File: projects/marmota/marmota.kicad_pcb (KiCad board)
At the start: 2 copper layers, 70 x 70 mm, 59 parts, among them J1 USB_C, J2 Conn_01x20_Pin, J3 Conn_01x20_Pin, SW1 Button top, SW2 Button side, U1 RP2040, U2 FLASH, U3 MCP73871, U4 RT6160, U5 ESP32, Y1 12MHz

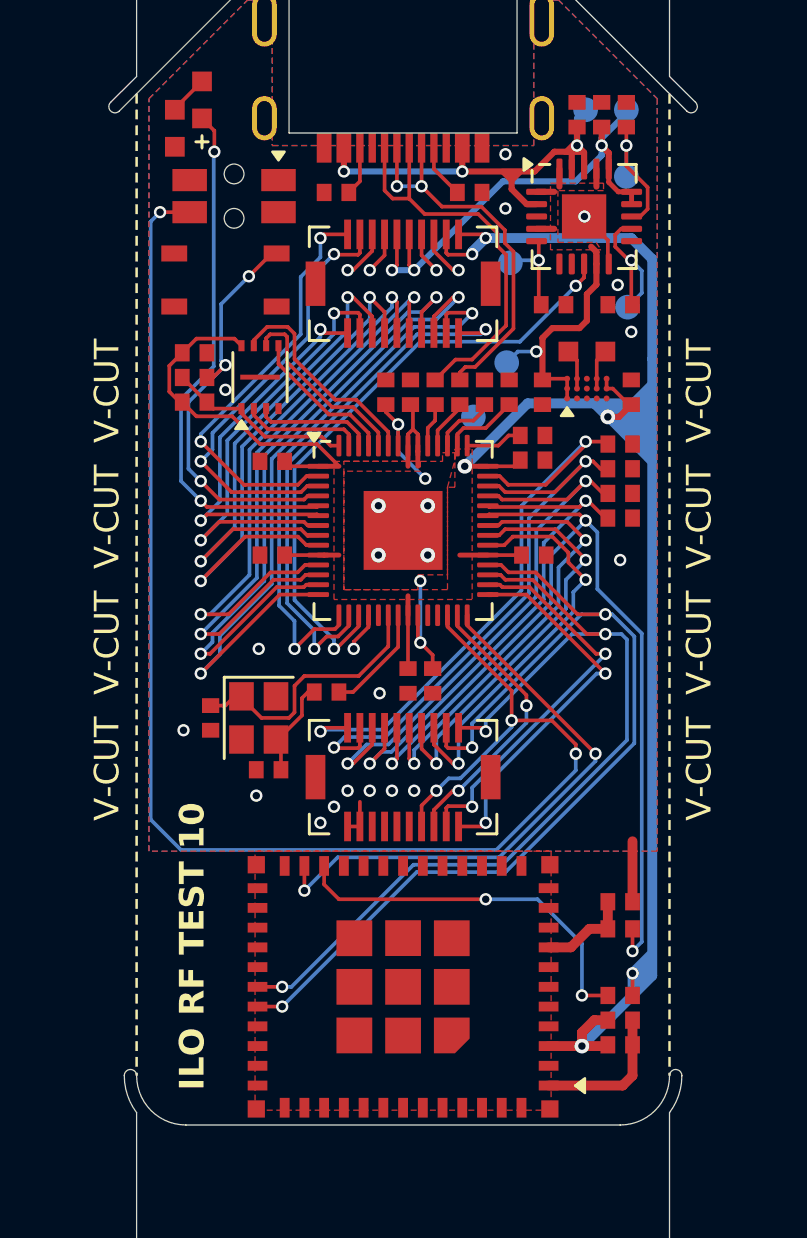
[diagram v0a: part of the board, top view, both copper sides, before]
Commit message: Voltage divider and read on the ESP, Thermal relief for the ESP
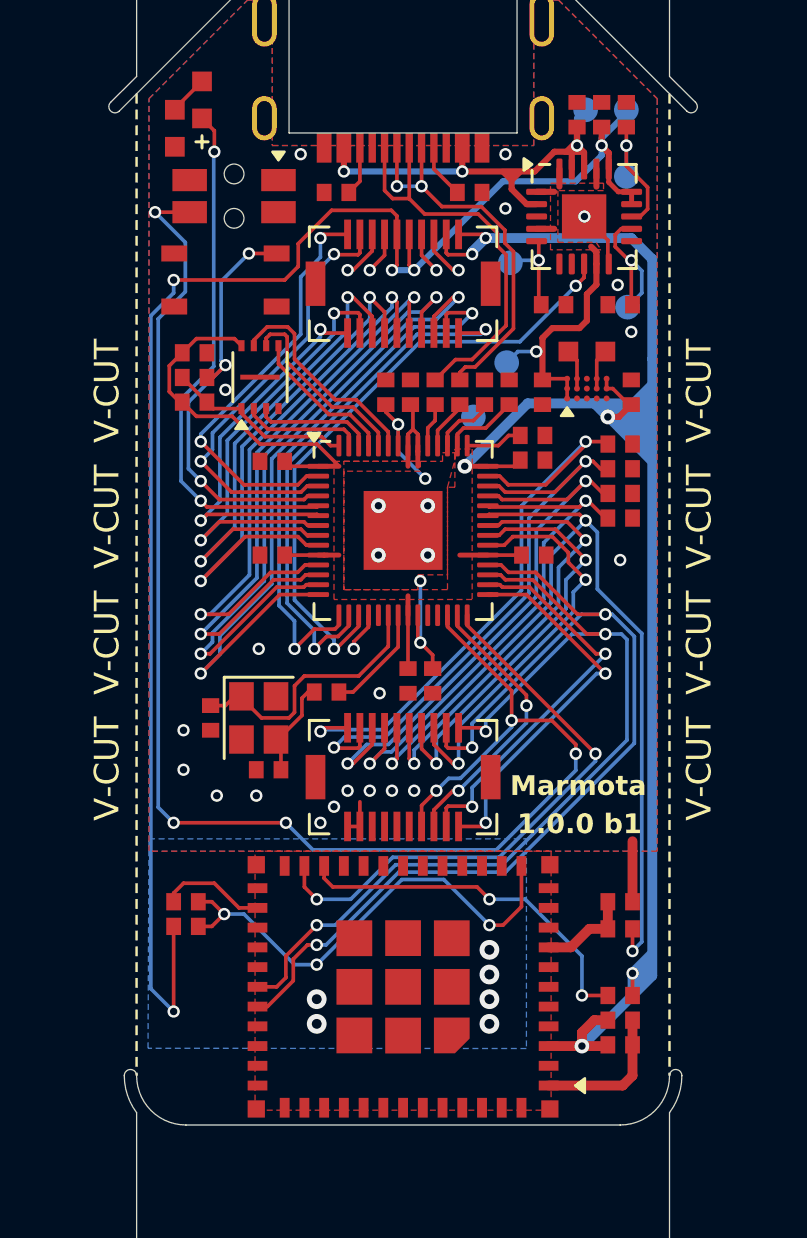
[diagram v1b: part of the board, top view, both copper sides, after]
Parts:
- added G***: LOGO, LOGO, B.Cu at (66.7, 66.5)
- added G***: LOGO, LOGO, B.Cu at (54.4, 64.2)
- added R52: 10KΩ, ILO_fp:0402_compact, F.Cu at (51.2, 68.0)
- added R53: 10KΩ, ILO_fp:0402_compact, F.Cu at (51.2, 67.0)
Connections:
- U5 pad 12: unconnected-(U5-IO0-Pad12) -> /EADC0
- U5 pad 26: unconnected-(U5-IO18-Pad26) -> /EGP18
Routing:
- net /BAT+: track 19.7 -> 65.2 mm, vias 3 -> 5
- net /EADC0: track 0.00 -> 19.6 mm, vias 0 -> 3
- net /EGP18: track 0.00 -> 4.33 mm
- net /UART1_TX: track 37.8 -> 38.3 mm
- net /UART1_RX: track 41.2 -> 41.7 mm
- net /RUN: track 60.8 -> 60.9 mm, vias 4 -> 6
- net GND: vias 23 -> 32
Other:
- board text added: "1.0.0 b1"
- board text added: "BY-NC-SA 4.0"
- board text added: "Input Labs Oy. Marmota 1.0.0 beta1"
- board text added: "Marmota"
- board text removed: "ILO RF TEST 10"

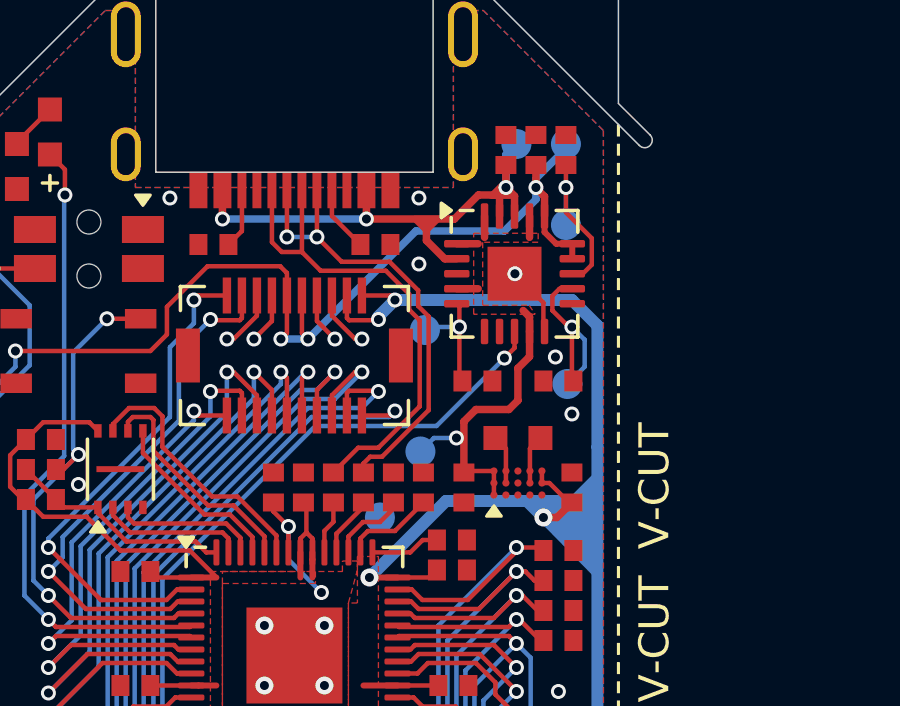
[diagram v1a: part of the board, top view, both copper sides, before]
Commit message: New arrangement for buckboost, Added 2nd vcc capacitor
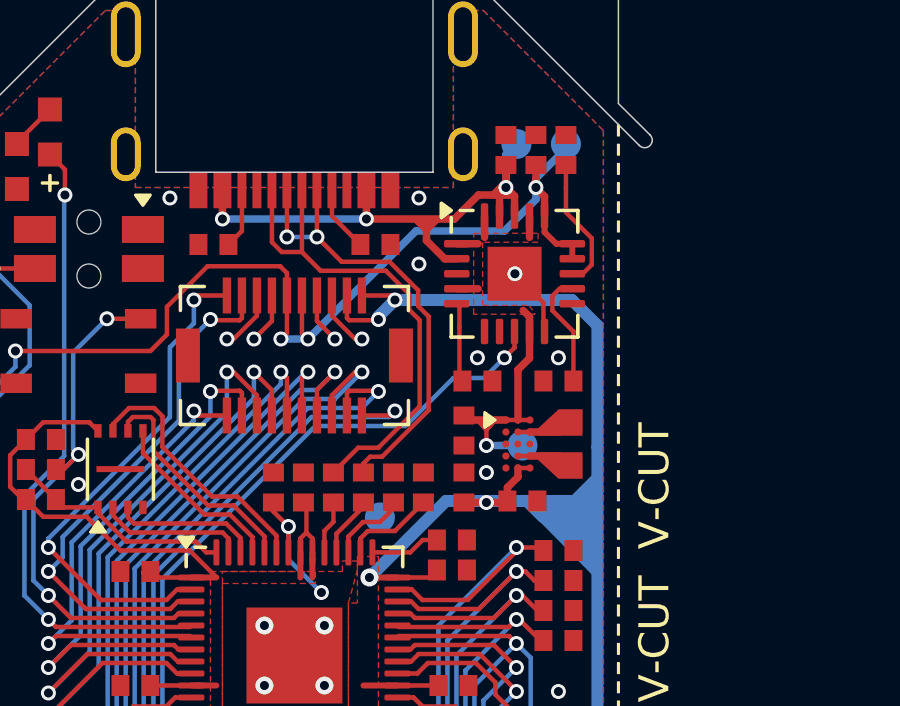
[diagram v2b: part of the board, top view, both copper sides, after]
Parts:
- removed the REF** at (69.0, 37.6)
- removed the REF** at (64.3, 41.1)
- removed the REF** at (69.1, 43.0)
- added C43: 22uF, ILO_fp:0402_compact, F.Cu at (67.6, 46.9)
- moved C42 3.60 mm to (65.7, 46.4)
- moved REF** 3.41 mm to (67.6, 45.0)
- moved C41 1.90 mm to (65.7, 44.5)
- moved L1 1.76 mm to (69.2, 45.0), turned to -90 degrees
- moved U4 1.30 mm to (67.5, 45.0), turned to -90 degrees
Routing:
- net Net-(U3-PROG3): track 6.26 -> 3.89 mm, vias 1 -> 0
- net VSYS: track 13.3 -> 11.1 mm
- net Net-(U3-PROG1): track 5.71 -> 4.46 mm, vias 1 -> 0
- net Net-(U3-THERM): track 3.84 -> 2.65 mm, vias 1 -> 0
- net GND: vias 32 -> 33
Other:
- board text removed: "P1"
- board text removed: "P3"
- board text removed: "TH"

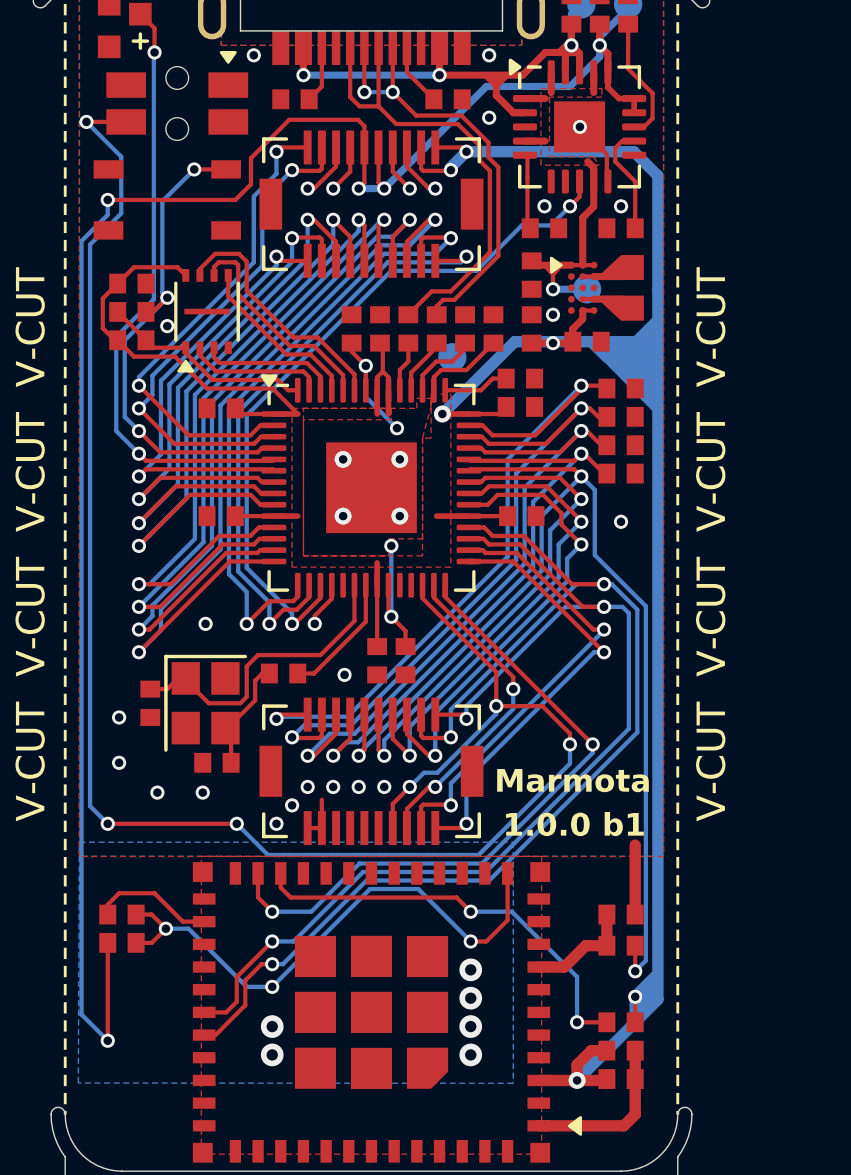
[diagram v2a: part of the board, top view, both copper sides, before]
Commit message: Added I2C pullups
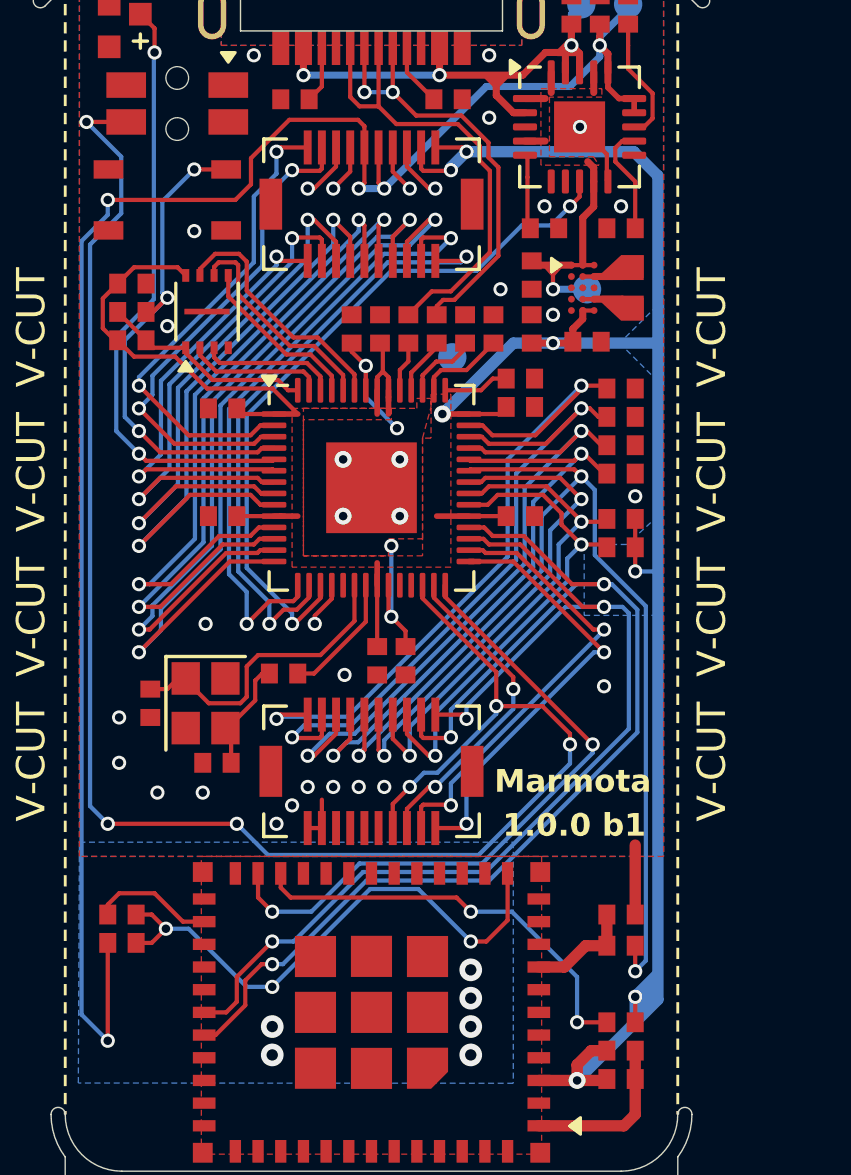
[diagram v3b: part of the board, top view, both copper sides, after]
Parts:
- added R7: 4.7KΩ, ILO_fp:0402_compact, F.Cu at (68.8, 54.1)
- added R8: 4.7KΩ, ILO_fp:0402_compact, F.Cu at (68.8, 53.1)
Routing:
- net +3V3: track 94.3 -> 98.2 mm, vias 6 -> 7
- net /I2C_SDA: track 16.6 -> 17.6 mm
- net /I2C_SCL: track 17.1 -> 18.0 mm
- net GND: vias 33 -> 36
- added copper zone on B.Cu, net +3V3

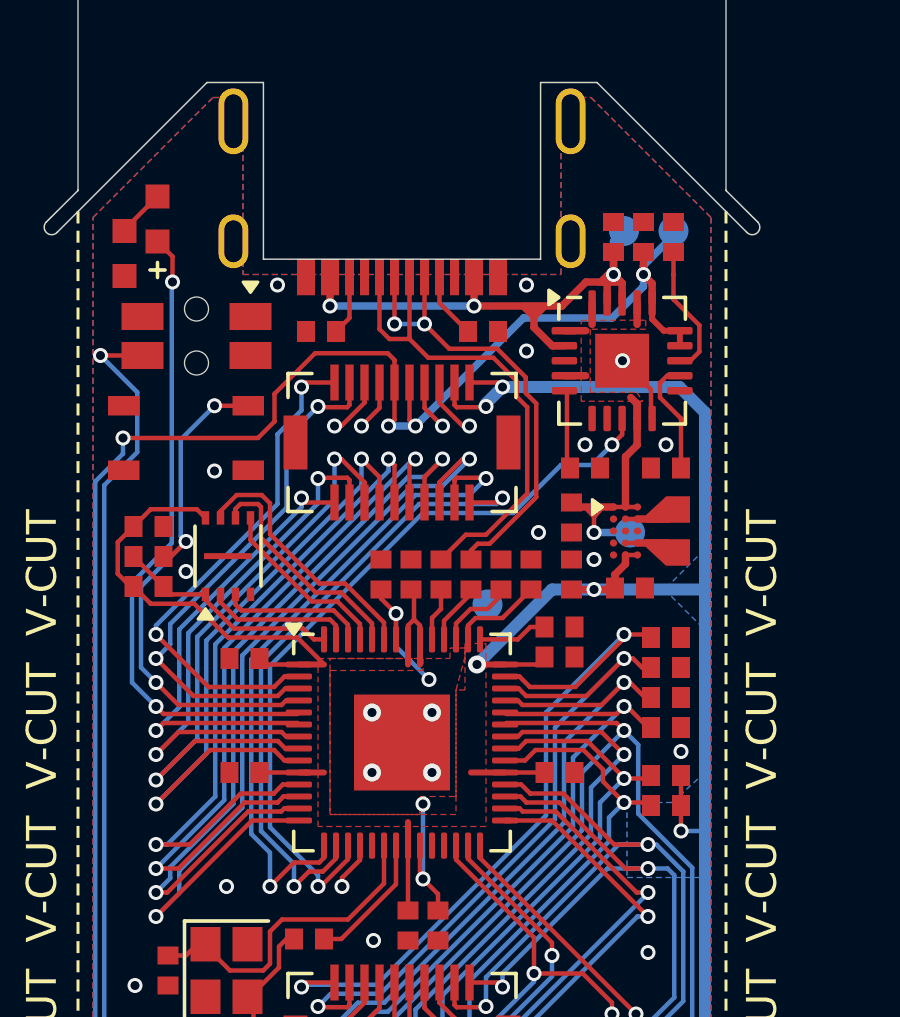
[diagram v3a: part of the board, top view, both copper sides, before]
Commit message: MCP without inner traces, Richtek rearrange
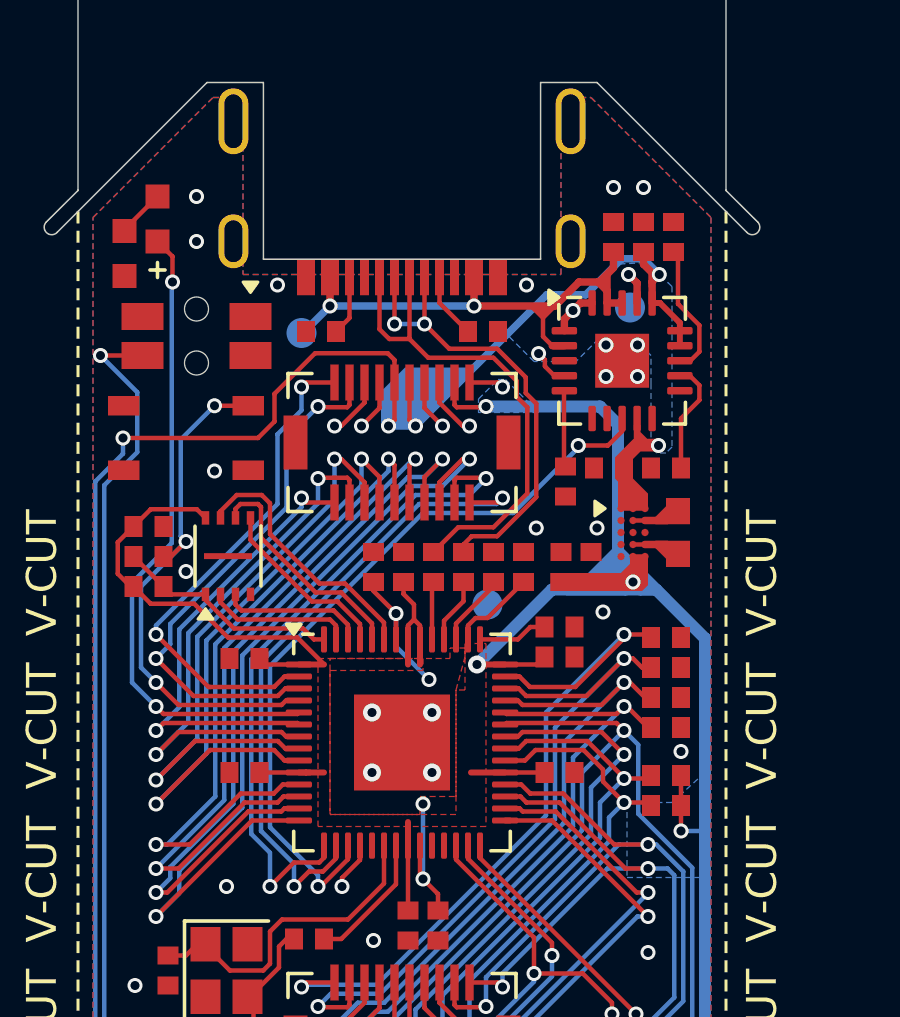
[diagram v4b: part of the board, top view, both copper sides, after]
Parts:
- moved REF** 11.3 mm to (56.6, 38.4)
- moved REF** 10.2 mm to (60.5, 40.4)
- moved REF** 7.50 mm to (67.6, 37.5)
- moved C41 2.07 mm to (66.9, 42.9), turned to 0 degrees
- moved C43 1.48 mm to (66.3, 46.1), turned to -90 degrees
- moved R34 0.79 mm to (65.5, 43.3), turned to -90 degrees
- moved C42 0.43 mm to (65.3, 46.1)
- moved C10 0.35 mm to (64.0, 46.1)
- moved C6 0.35 mm to (59.0, 46.1)
- moved C8 0.35 mm to (63.0, 46.1)
- moved C9 0.35 mm to (60.0, 46.1)
- moved R3 0.35 mm to (61.0, 46.1)
- moved R4 0.35 mm to (62.0, 46.1)
- moved U4 0.25 mm to (67.7, 45.0)
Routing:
- net +3V3: track 98.2 -> 90.3 mm
- net VSYS: track 11.1 -> 4.70 mm, vias 1 -> 4
- net GND: track 15.9 -> 13.7 mm, vias 36 -> 41
- net VBUS: track 17.8 -> 16.6 mm, vias 3 -> 2
- net /BAT+: track 65.2 -> 64.2 mm
- added copper zone on B.Cu, net VSYS
- removed copper zone on F.Cu, net VSYS
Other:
- board text added: "VBUS"
- board text removed: "VB"

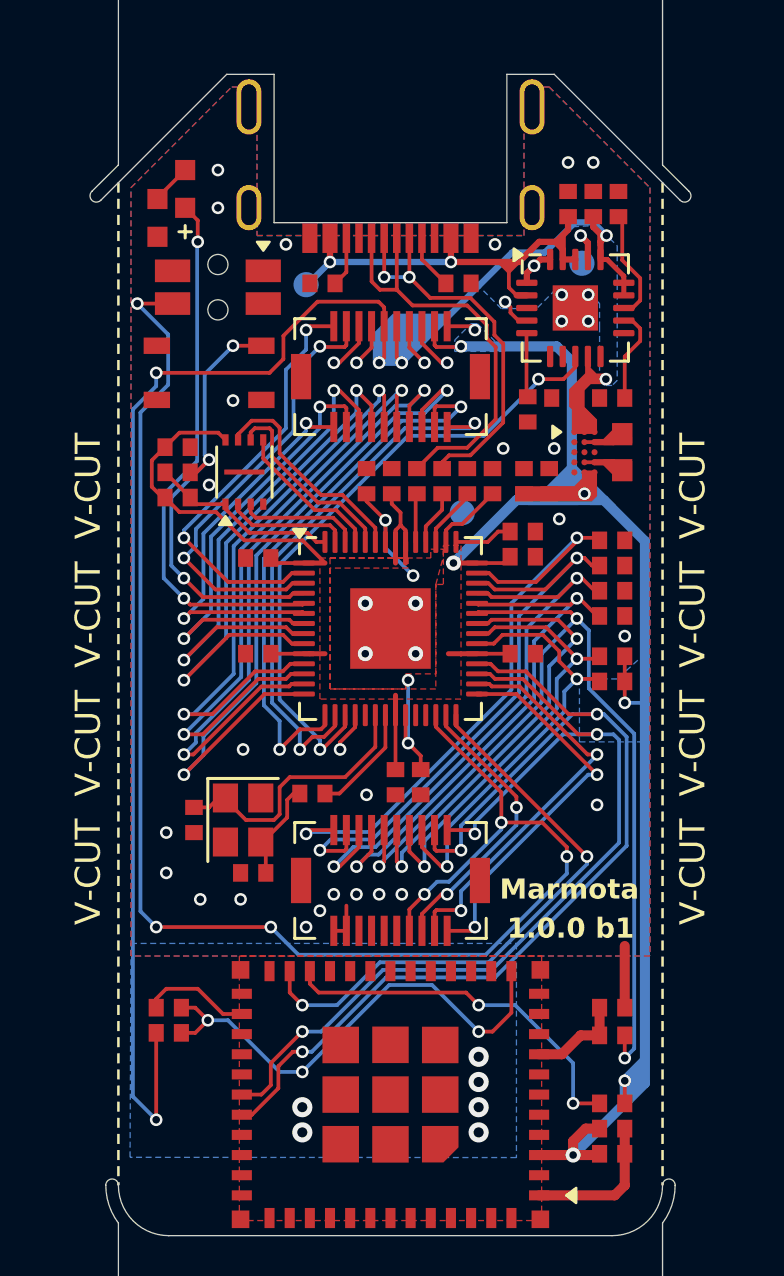
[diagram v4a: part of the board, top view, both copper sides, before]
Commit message: Bigger footprint inductor
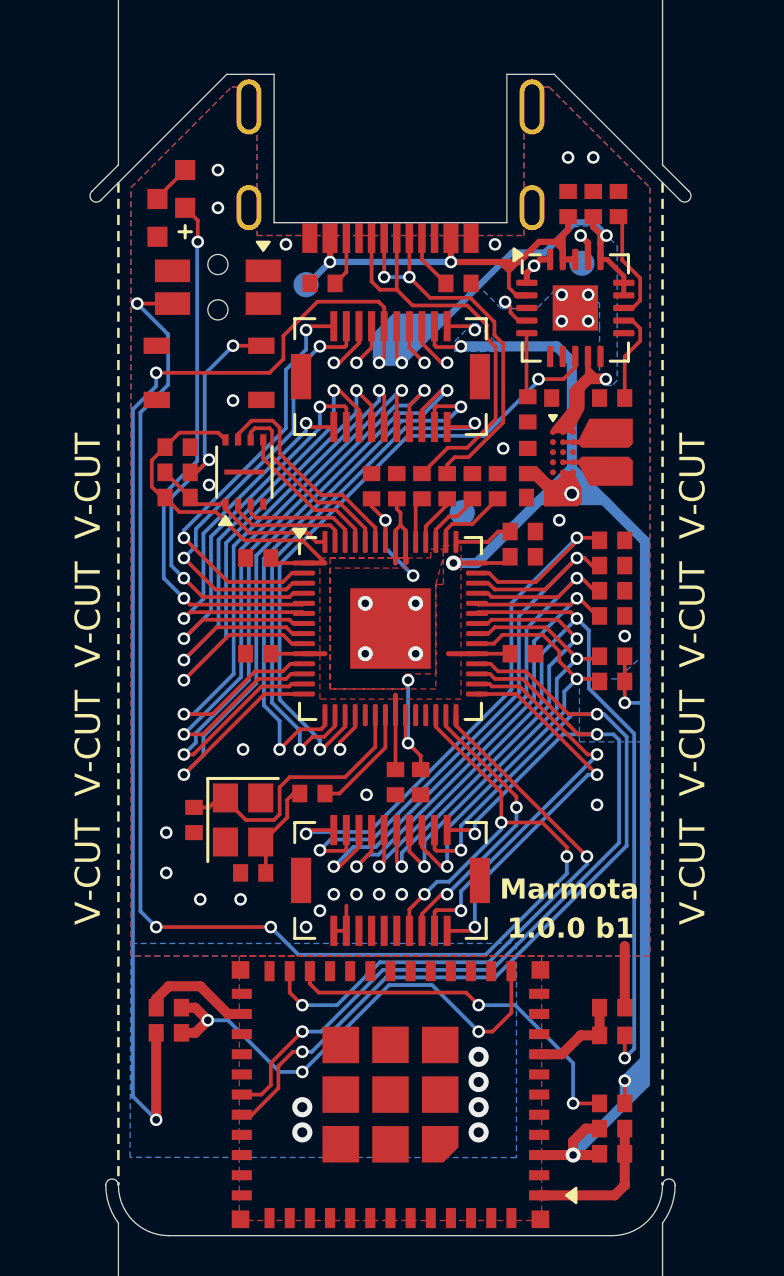
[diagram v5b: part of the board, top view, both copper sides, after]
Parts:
- L1: footprint ILO_fp:0603_compact -> ILO_fp:SMD_16x10
- moved U4 0.85 mm to (66.8, 45.0)
- moved C42 0.81 mm to (65.5, 45.4)
- moved C43 0.76 mm to (65.9, 46.8), turned to 0 degrees
- moved L1 0.45 mm to (68.8, 45.0), turned to 90 degrees
- moved C10 0.28 mm to (64.2, 46.4)
- moved C6 0.28 mm to (59.2, 46.4)
- moved C8 0.28 mm to (63.2, 46.4)
- moved C9 0.28 mm to (60.2, 46.4)
- moved R3 0.28 mm to (61.2, 46.4)
- moved R4 0.28 mm to (62.2, 46.4)
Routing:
- net Net-(L1-Pad2): track 1.64 -> 0.40 mm
- net Net-(L1-Pad1): track 1.64 -> 0.40 mm
- net VSYS: track 4.70 -> 3.90 mm
- net +3V3: track 90.3 -> 89.8 mm
- net GND: vias 41 -> 40
